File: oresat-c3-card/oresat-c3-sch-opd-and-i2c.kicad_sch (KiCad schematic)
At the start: 37 parts, among them Q1 DMP2035UQ-7, U12 RCLAMP0504FB, U13 MAX892LEUA+T, U24 RV-3028-C7, U30 FM24CL64B-GTR, U37 LTC4300A-1

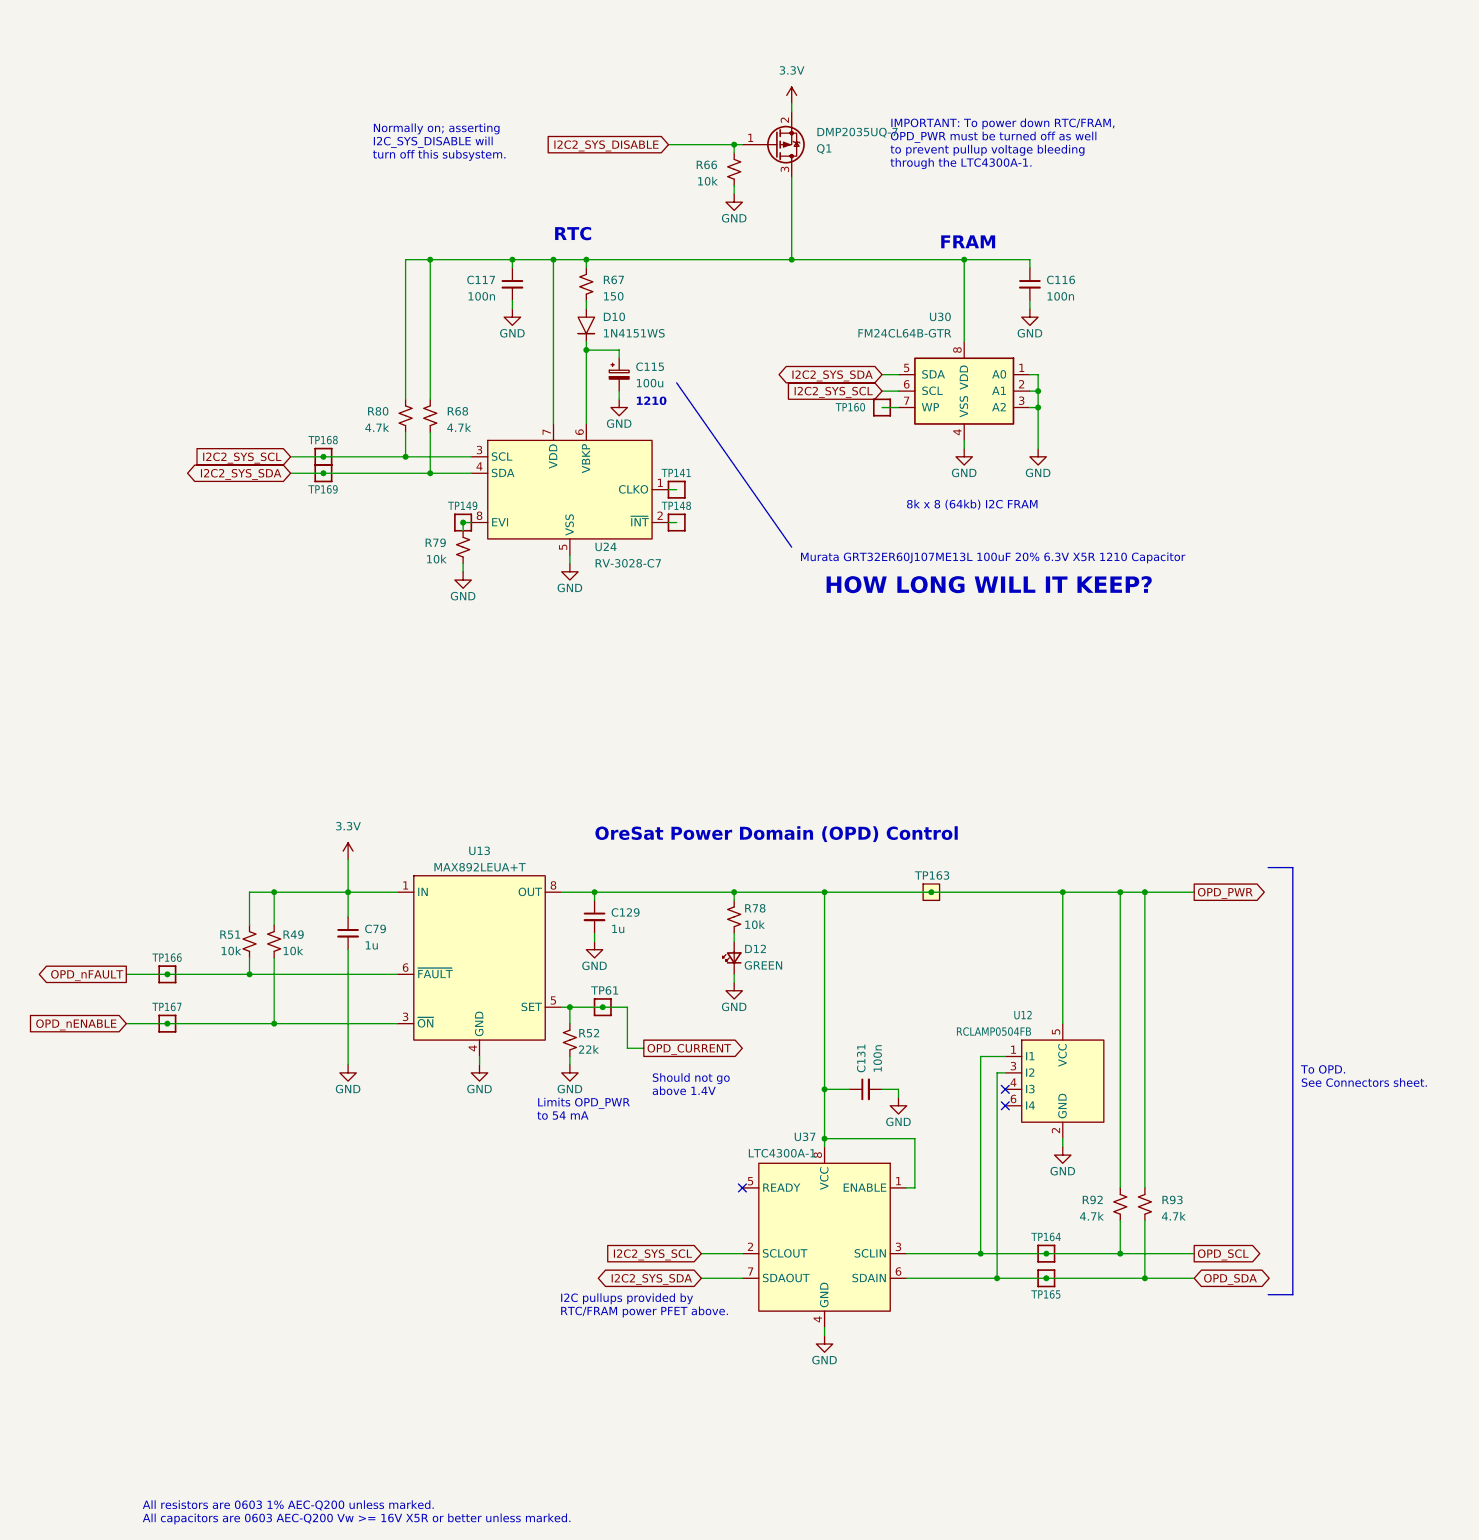
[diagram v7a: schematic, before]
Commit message: All DRC exclusing RF traces are cleaned up.  RF traces cleaned up with mask and bends. Some more notes in the schematic for future us.
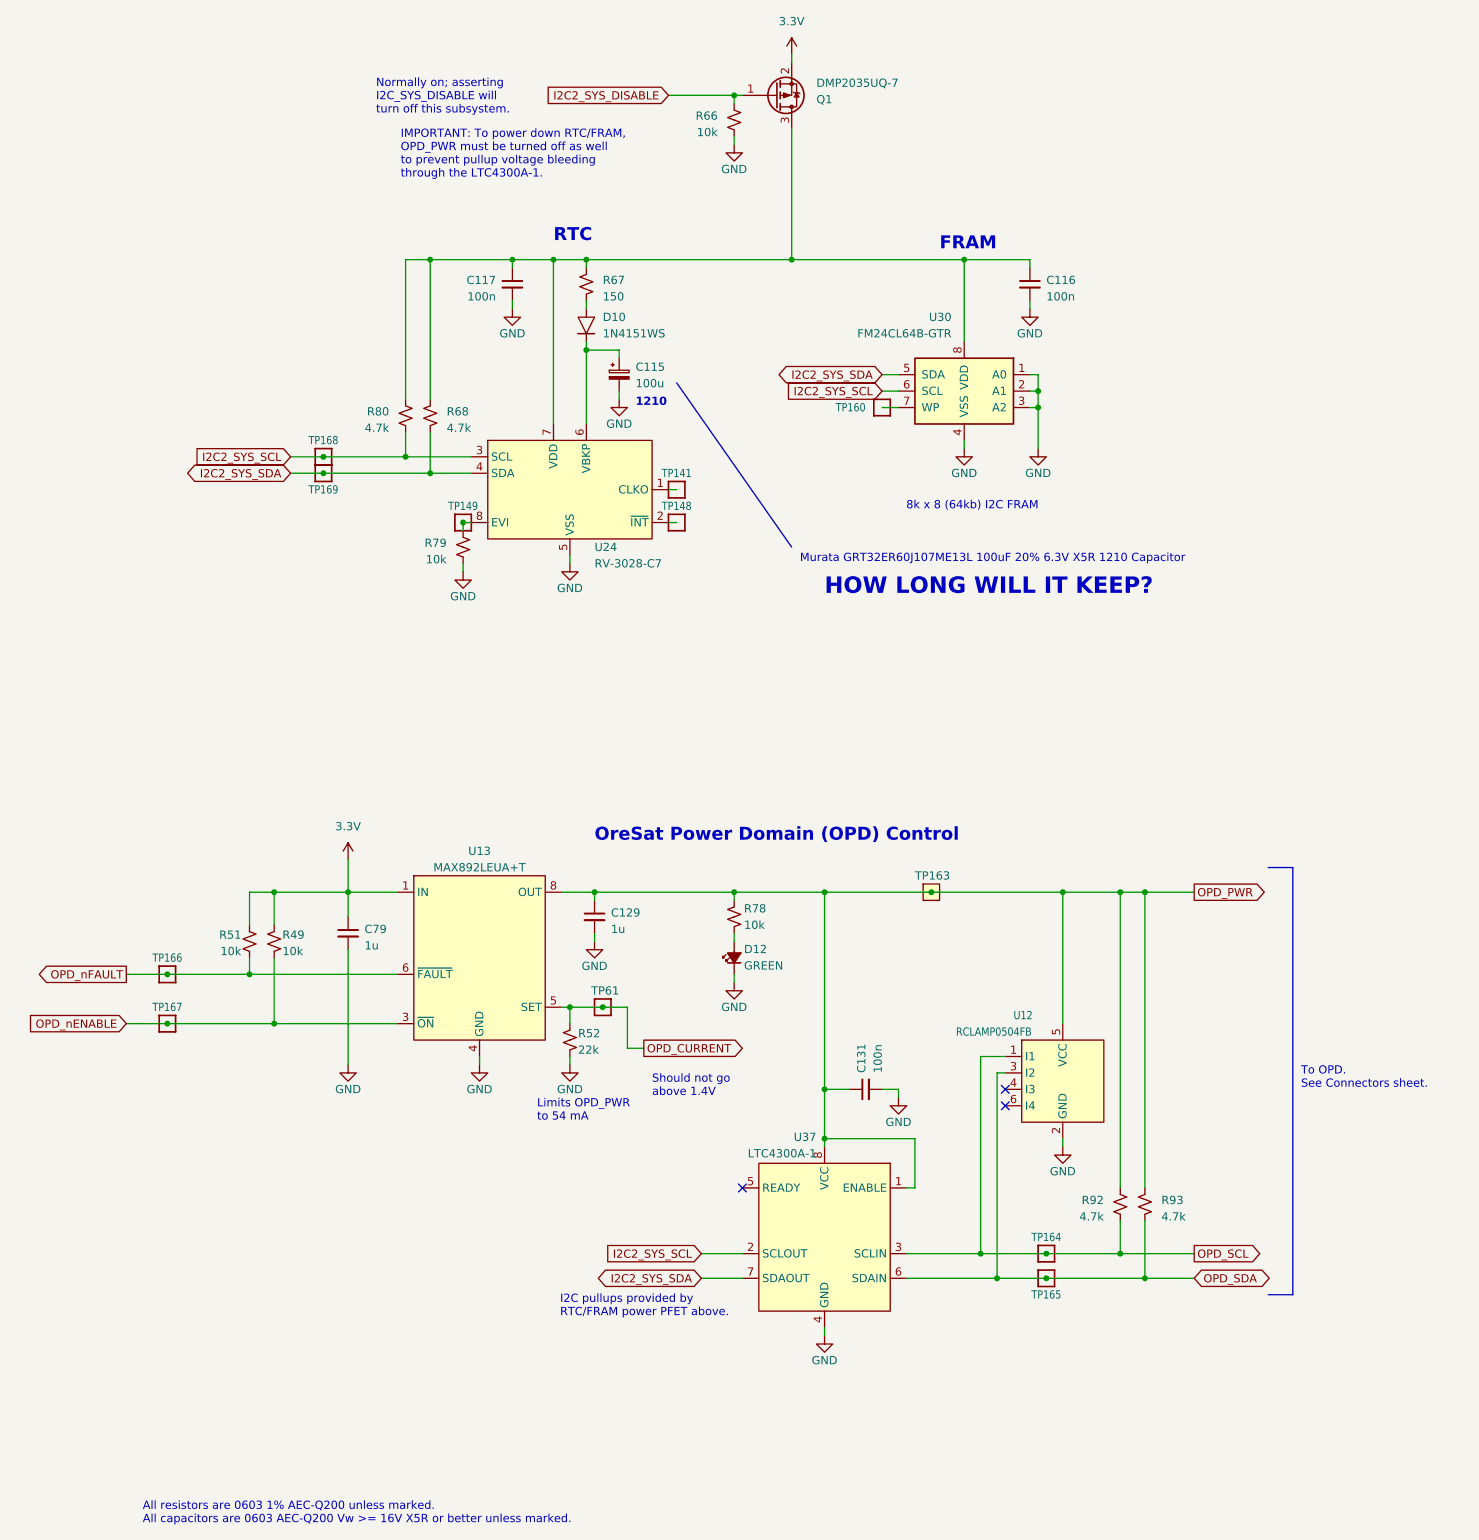
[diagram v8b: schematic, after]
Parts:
- D12: symbol Device:LED_Small -> Device:LED_Small_Filled
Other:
- moved on the sheet: Q1, R66
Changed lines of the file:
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@@
 	(text "Normally on; asserting \nI2C_SYS_DISABLE will \nturn off this subsystem."
 		(exclude_from_sim no)
-		(at 151.13 50.8 0)
+		(at 151.638 43.688 0)
 		(effects
 			(font
@@
 	(text "IMPORTANT: To power down RTC/FRAM,\nOPD_PWR must be turned off as well\nto prevent pullup voltage bleeding\nthrough the LTC4300A-1."
 		(exclude_from_sim no)
-		(at 231.14 52.07 0)
+		(at 155.448 53.594 0)
 		(effects
 			(font
@@
 	)
 	(junction
-		(at 207.01 48.26)
+		(at 207.01 40.64)
 		(diameter 0)
 		(color 0 0 0 0)
@@
 	(wire
 		(pts
-			(xy 207.01 48.26) (xy 207.01 49.53)
+			(xy 207.01 40.64) (xy 207.01 41.91)
 		)
 		(stroke
@@
 	(wire
 		(pts
-			(xy 215.9 53.34) (xy 215.9 66.04)
+			(xy 215.9 45.72) (xy 215.9 66.04)
 		)
 		(stroke
@@
 	(wire
 		(pts
-			(xy 207.01 54.61) (xy 207.01 55.88)
+			(xy 207.01 46.99) (xy 207.01 48.26)
 		)
 		(stroke
@@
 	(wire
 		(pts
-			(xy 215.9 41.91) (xy 215.9 43.18)
+			(xy 215.9 34.29) (xy 215.9 35.56)
 		)
 		(stroke
@@
 	(wire
 		(pts
-			(xy 196.85 48.26) (xy 207.01 48.26)
+			(xy 196.85 40.64) (xy 207.01 40.64)
 		)
 		(stroke
@@
 	(wire
 		(pts
-			(xy 207.01 48.26) (xy 208.28 48.26)
+			(xy 207.01 40.64) (xy 208.28 40.64)
 		)
 		(stroke
@@
 	(global_label "I2C2_SYS_DISABLE"
 		(shape input)
-		(at 196.85 48.26 180)
+		(at 196.85 40.64 180)
 		(fields_autoplaced yes)
 		(effects
@@
 		)
 		(property "Intersheetrefs" "${INTERSHEET_REFS}"
-			(at 176.5876 48.26 0)
+			(at 176.5876 40.64 0)
 			(effects
 				(font
@@
 	(symbol
 		(lib_id "Device:R_Small_US")
-		(at 207.01 52.07 0)
+		(at 207.01 44.45 0)
 		(unit 1)
 		(exclude_from_sim no)
@@
 		(dnp no)
 		(property "Reference" "R66"
-			(at 204.47 51.435 0)
+			(at 204.47 43.815 0)
 			(effects
 				(font
@@
 		)
 		(property "Value" "10k"
-			(at 204.47 53.975 0)
+			(at 204.47 46.355 0)
 			(effects
 				(font
@@
 		)
 		(property "Footprint" "oresat-passives:0603-C-NOSILK"
-			(at 207.01 52.07 0)
+			(at 207.01 44.45 0)
 			(effects
 				(font
@@
 		)
 		(property "Datasheet" "https://www.seielect.com/catalog/SEI-RMCF_RMCP.pdf"
-			(at 207.01 52.07 0)
+			(at 207.01 44.45 0)
 			(effects
 				(font
@@
 		)
 		(property "Description" "10 kOhms ±1% 0.1W, 1/10W Chip Resistor 0603 (1608 Metric) Automotive AEC-Q200 Thick Film"
-			(at 207.01 52.07 0)
+			(at 207.01 44.45 0)
 			(effects
 				(font
@@
 		)
 		(property "DPN" "RMCF0603FT10K0CT-ND"
-			(at 207.01 52.07 0)
+			(at 207.01 44.45 0)
 			(effects
 				(font
@@
 		)
 		(property "DST" "DigiKey"
-			(at 207.01 52.07 0)
+			(at 207.01 44.45 0)
 			(effects
 				(font
@@
 		)
 		(property "MFR" "Stackpole Electronics"
-			(at 207.01 52.07 0)
+			(at 207.01 44.45 0)
 			(effects
 				(font
@@
 		)
 		(property "MPN" "RMCF0603FT10K0"
-			(at 207.01 52.07 0)
+			(at 207.01 44.45 0)
 			(effects
 				(font
@@
 	(symbol
 		(lib_id "Transistor_FET:NTR2101P")
-		(at 213.36 48.26 0)
+		(at 213.36 40.64 0)
 		(mirror x)
 		(unit 1)
@@
 		(dnp no)
 		(property "Reference" "Q1"
-			(at 219.71 48.895 0)
+			(at 219.71 41.275 0)
 			(effects
 				(font
@@
 		)
 		(property "Value" "DMP2035UQ-7"
-			(at 219.71 46.355 0)
+			(at 219.71 38.735 0)
 			(effects
 				(font
@@
 		)
 		(property "Footprint" "Package_TO_SOT_SMD:SOT-23"
-			(at 218.44 46.355 0)
+			(at 218.44 38.735 0)
 			(effects
 				(font
@@
 		)
 		(property "Datasheet" "https://www.diodes.com/assets/Datasheets/DMP2035U.pdf"
-			(at 213.36 48.26 0)
+			(at 213.36 40.64 0)
 			(effects
 				(font
@@
 		)
 		(property "Description" "P-Channel 20 V 4.9A (Ta) 810mW (Ta) Surface Mount SOT-23-3 (TO-236)"
-			(at 213.36 48.26 0)
+			(at 213.36 40.64 0)
 			(effects
 				(font
@@
 		)
 		(property "DPN" "31-DMP2035UQ-7CT-ND"
-			(at 213.36 48.26 0)
+			(at 213.36 40.64 0)
 			(effects
 				(font
@@
 		)
 		(property "DST" "DigiKey"
-			(at 213.36 48.26 0)
+			(at 213.36 40.64 0)
 			(effects
 				(font
@@
 		)
 		(property "MFR" "Diodes Incorporated"
-			(at 213.36 48.26 0)
+			(at 213.36 40.64 0)
 			(effects
 				(font
@@
 		)
 		(property "MPN" "DMP2035UQ-7"
-			(at 213.36 48.26 0)
+			(at 213.36 40.64 0)
 			(effects
 				(font
@@
 	)
 	(symbol
-		(lib_id "Device:LED_Small")
+		(lib_id "Device:LED_Small_Filled")
 		(at 207.01 173.99 90)
 		(unit 1)
@@
 			)
 		)
-		(property "Datasheet" "https://www.we-online.com/components/products/datasheet/150060GS75000.pdf"
+		(property "Datasheet" "~"
 			(at 207.01 173.99 90)
 			(effects
@@
 			)
 		)
-		(property "Description" "Green 520nm LED Indication - Discrete 3.2V 0603 (1608 Metric) - 430 mcd @ 20 mA"
+		(property "Description" "Light emitting diode, small symbol, filled shape"
 			(at 207.01 173.99 0)
 			(effects
@@
 	(symbol
 		(lib_id "oresat-power:3.3V")
-		(at 215.9 41.91 0)
+		(at 215.9 34.29 0)
 		(unit 1)
 		(exclude_from_sim no)
@@
 		(fields_autoplaced yes)
 		(property "Reference" "#3V01"
-			(at 215.9 45.72 0)
+			(at 215.9 38.1 0)
 			(effects
 				(font
@@
 		)
 		(property "Value" "3.3V"
-			(at 215.9 36.83 0)
+			(at 215.9 29.21 0)
 			(effects
 				(font
@@
 		)
 		(property "Footprint" ""
-			(at 215.9 41.91 0)
+			(at 215.9 34.29 0)
 			(effects
 				(font
@@
 		)
 		(property "Datasheet" ""
-			(at 215.9 41.91 0)
+			(at 215.9 34.29 0)
 			(effects
 				(font
@@
 		)
 		(property "Description" ""
-			(at 215.9 41.91 0)
+			(at 215.9 34.29 0)
 			(effects
 				(font
@@
 	(symbol
 		(lib_id "power:GND")
-		(at 207.01 55.88 0)
+		(at 207.01 48.26 0)
 		(unit 1)
 		(exclude_from_sim no)
@@
 		(dnp no)
 		(property "Reference" "#PWR0280"
-			(at 207.01 62.23 0)
+			(at 207.01 54.61 0)
 			(effects
 				(font
@@
 		)
 		(property "Value" "GND"
-			(at 207.01 59.69 0)
+			(at 207.01 52.07 0)
 			(effects
 				(font
@@
 		)
 		(property "Footprint" ""
-			(at 207.01 55.88 0)
+			(at 207.01 48.26 0)
 			(effects
 				(font
@@
 		)
 		(property "Datasheet" ""
-			(at 207.01 55.88 0)
+			(at 207.01 48.26 0)
 			(effects
 				(font
@@
 		)
 		(property "Description" "Power symbol creates a global label with name \"GND\" , ground"
-			(at 207.01 55.88 0)
+			(at 207.01 48.26 0)
 			(effects
 				(font
